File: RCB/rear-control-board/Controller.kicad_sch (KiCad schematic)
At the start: 23 parts, among them J6 Conn_01x05, U1 STM32F413CGUx, U2 LD1117S33TR_SOT223, U4 MCP2551-I-SN, Y1 CSTNE8M00

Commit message: willem review notes
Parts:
- added R?: 0, symbol Device:R
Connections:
- net +3V3: no longer U4.3 (VDD)
- net GND: now also R?.1; no longer U1.44 (BOOT0)
- new net: R?.2, U1.44 (BOOT0)
- new net +5V: U4.3 (VDD)
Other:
- note added: "Change these, the voltage divider stuff will be on the fault latcher sheet"
- note added: "add NC pins"
- note added: "add tsv to every signal pin including CAN -> use NUP2105LT1G or similar alternate The transceiver may have this built in, so double check"
- note added: "change to tx and rx and don't do differential pair"
- note added: "check pins for 5v tolerance actually, just do a different transceiver"
- note added: "check pull down value with ntc"
- note added: "choose a different tranceiver - one that has a vio pin that can set voltage - 3v tranceiver - level shifter - open drain on stm32 and pull up to 5v Look at MAX33054EASA+T"
- note added: "double check datasheet probably don't need this"
- note added: "header: FTSH-105-01-F-DV-K"
- note added: "seprate out ground and make it look pretty"
- note added: "vdd is 5v"
- note added: "why is is bold??"
- moved on the sheet: R4, R7

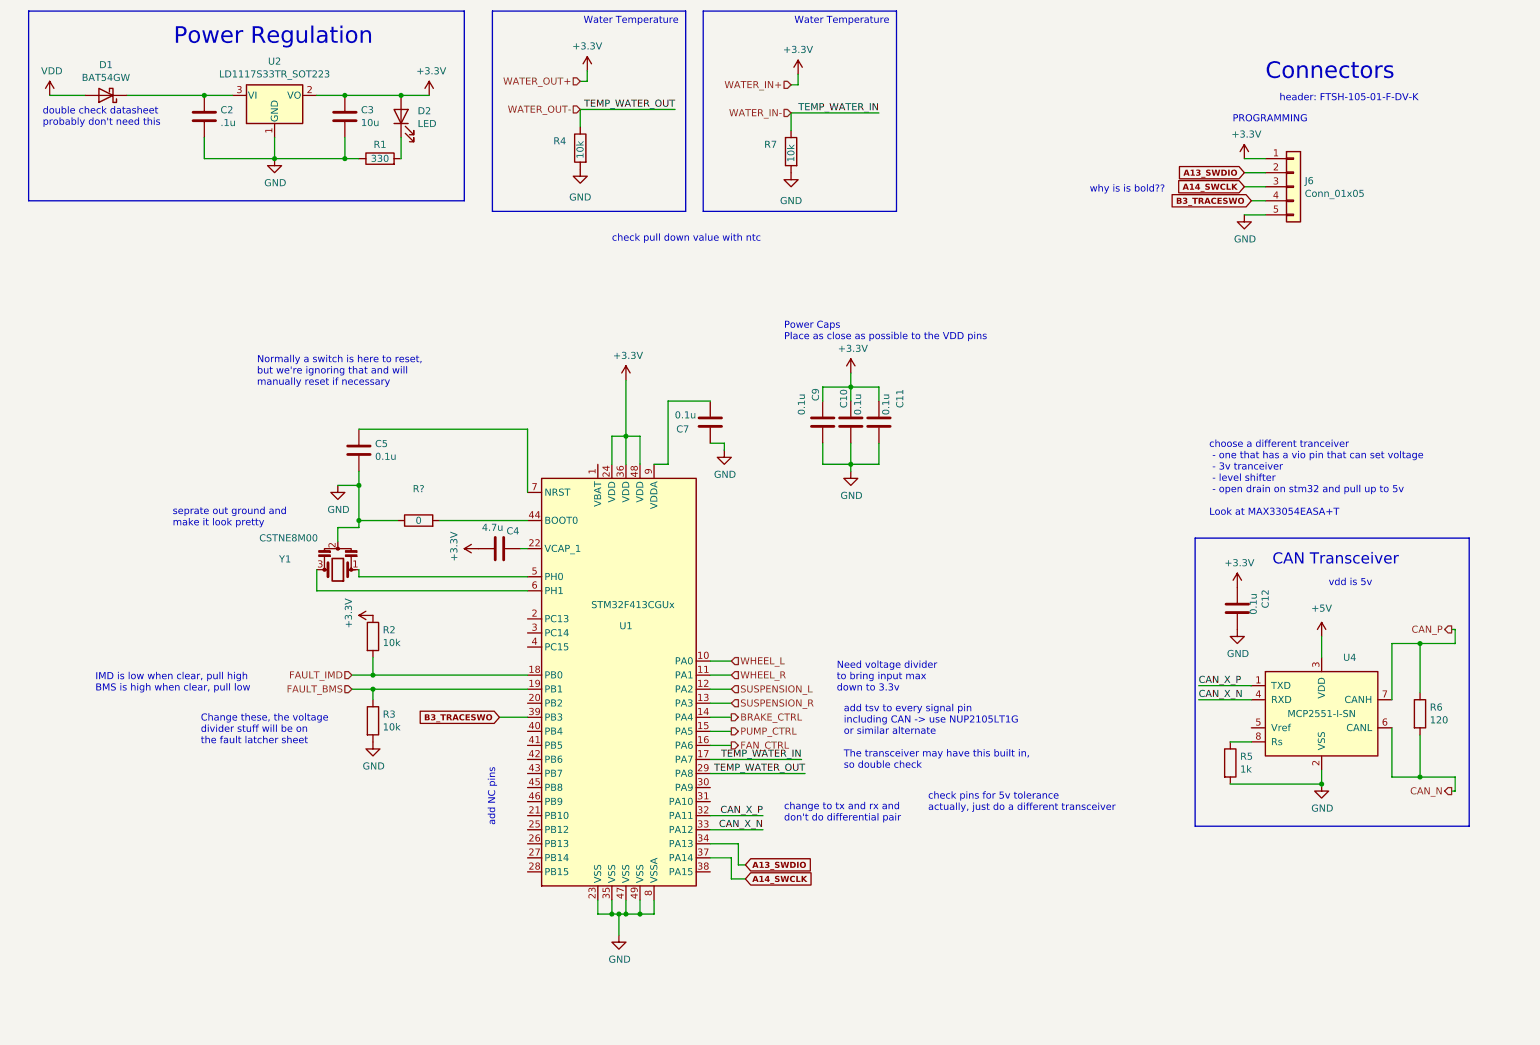
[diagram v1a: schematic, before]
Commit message: updating schem with design notes (major changes)
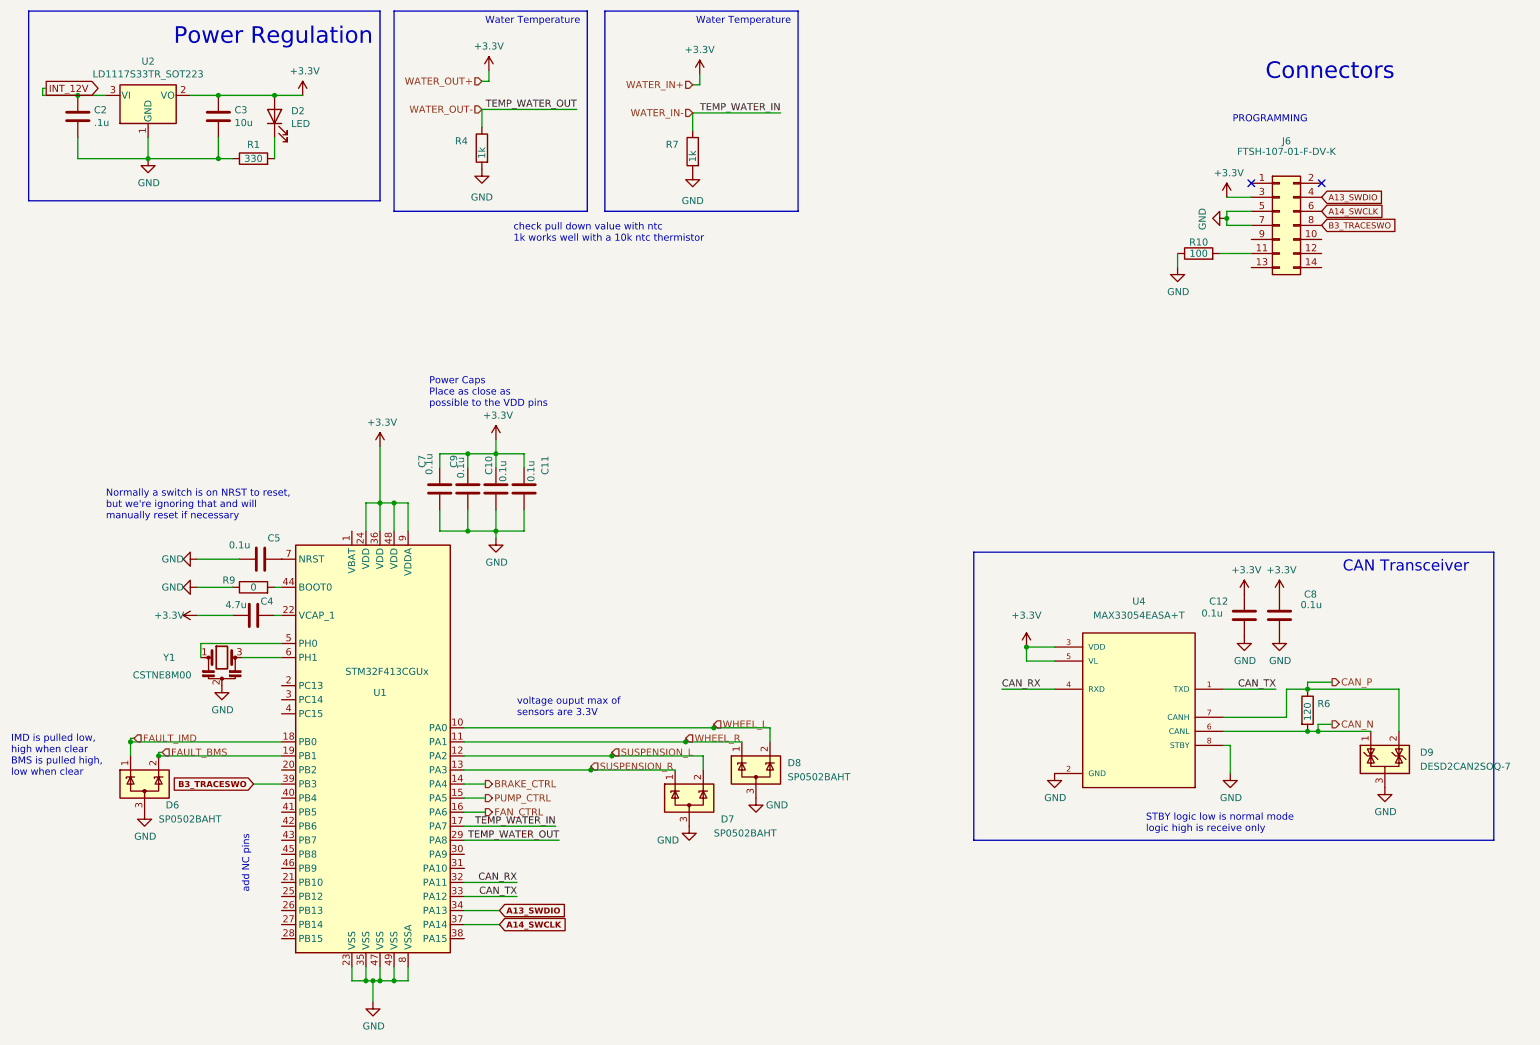
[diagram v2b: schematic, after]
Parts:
- removed D1: BAT54GW, Diode_SMD:D_SMB, symbol Device:D_Schottky
- removed J6: Conn_01x05, Connector_JST:JST_XH_B5B-XH-A_1x05_P2.50mm_Vertical, symbol Connector_Generic:Conn_01x05
- removed R2, R3: 10k, Resistor_SMD:R_0603_1608Metric_Pad0.98x0.95mm_HandSolder, symbol Device:R
- removed R5: 1k, Resistor_SMD:R_0603_1608Metric_Pad0.98x0.95mm_HandSolder, symbol Device:R
- removed U4: MCP2551-I-SN, Package_SO:SOIC-8_3.9x4.9mm_P1.27mm, symbol Interface_CAN_LIN:MCP2551-I-SN
- added C8: 0.1u, Capacitor_SMD:C_0603_1608Metric_Pad1.08x0.95mm_HandSolder, symbol Device:C
- added D6, D7, D8: SP0502BAHT, Package_TO_SOT_SMD:SOT-23, symbol Power_Protection:SP0502BAHT
- added D9: DESD2CAN2SOQ-7, Package_TO_SOT_SMD:SOT-23, symbol Power_Protection:NUP2105L
- added J6: FTSH-107-01-F-DV-K, Connector_PinHeader_1.27mm:PinHeader_2x07_P1.27mm_Vertical_SMD, symbol Connector_Generic:Conn_02x07_Odd_Even
- added R10: 100, Resistor_SMD:R_0603_1608Metric_Pad0.98x0.95mm_HandSolder, symbol Device:R
- added U4: MAX33054EASA+T, AERO_Footprints:SOIC127P600X175-8N, symbol AERO_Symbols:MAX33054EASA+T
- R4, R7: value 10k -> 1k
- R9: renamed from R?; footprint (none) -> Resistor_SMD:R_0603_1608Metric_Pad0.98x0.95mm_HandSolder
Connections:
- net +3V3: now also C7.1, U1.9 (VDDA), C8.1, J6.3 (Pin_3), U4.3 (VDD), U4.5 (VL)
- net A13_SWDIO: now also J6.4 (Pin_4)
- net A14_SWCLK: now also J6.6 (Pin_6)
- net B3_TRACESWO: now also J6.8 (Pin_8)
- net CAN_N: now also D9.1 (K), U4.6 (CANL)
- net CAN_P: now also D9.2 (K), U4.7 (CANH)
- net FAULT_BMS: now also D6.2 (K)
- net FAULT_IMD: now also D6.1 (K)
- net GND: now also C7.2, C8.2, D6.3 (A), D7.3 (A), D8.3 (A), D9.3 (A), J6.5 (Pin_5), J6.7 (Pin_7), R10.1, U4.2 (GND), U4.8 (STBY); no longer C7.1
- net SUSPENSION_L: now also D7.2 (K)
- net SUSPENSION_R: now also D7.1 (K)
- net WHEEL_L: now also D8.2 (K)
- net WHEEL_R: now also D8.1 (K)
- net INT_12V: now reaches C2.1, U2.3 (VI)
- net CAN_X_N renamed CAN_TX
- net CAN_TX: now also U4.1 (TXD)
- net CAN_X_P renamed CAN_RX
- net CAN_RX: now also U4.4 (RXD)
- new net: J6.11 (Pin_11), R10.2
- no-connect marks 0 -> 2
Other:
- note added: "IMD is pulled low, high when clear BMS is pulled high, low when clear"
- note added: "Normally a switch is on NRST to reset, but we're ignoring that and will manually reset if necessary"
- note added: "STBY logic low is normal mode logic high is receive only"
- note added: "check pull down value with ntc 1k works well with a 10k ntc thermistor"
- note added: "voltage ouput max of sensors are 3.3V"
- note removed: "Change these, the voltage divider stuff will be on the fault latcher sheet"
- note removed: "IMD is low when clear, pull high BMS is high when clear, pull low"
- note removed: "Need voltage divider to bring input max down to 3.3v"
- note removed: "Normally a switch is here to reset, but we're ignoring that and will manually reset if necessary"
- note removed: "add tsv to every signal pin including CAN -> use NUP2105LT1G or similar alternate The transceiver may have this built in, so double check"
- note removed: "change to tx and rx and don't do differential pair"
- note removed: "check pins for 5v tolerance actually, just do a different transceiver"
- note removed: "check pull down value with ntc"
- note removed: "choose a different tranceiver - one that has a vio pin that can set voltage - 3v tranceiver - level shifter - open drain on stm32 and pull up to 5v Look at MAX33054EASA+T"
- note removed: "double check datasheet probably don't need this"
- note removed: "header: FTSH-105-01-F-DV-K"
- note removed: "seprate out ground and make it look pretty"
- note removed: "vdd is 5v"
- note removed: "why is is bold??"
- moved on the sheet: C10, C11, C12, C2, C3, C4, C5, C9, D2, R1, R4, R6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

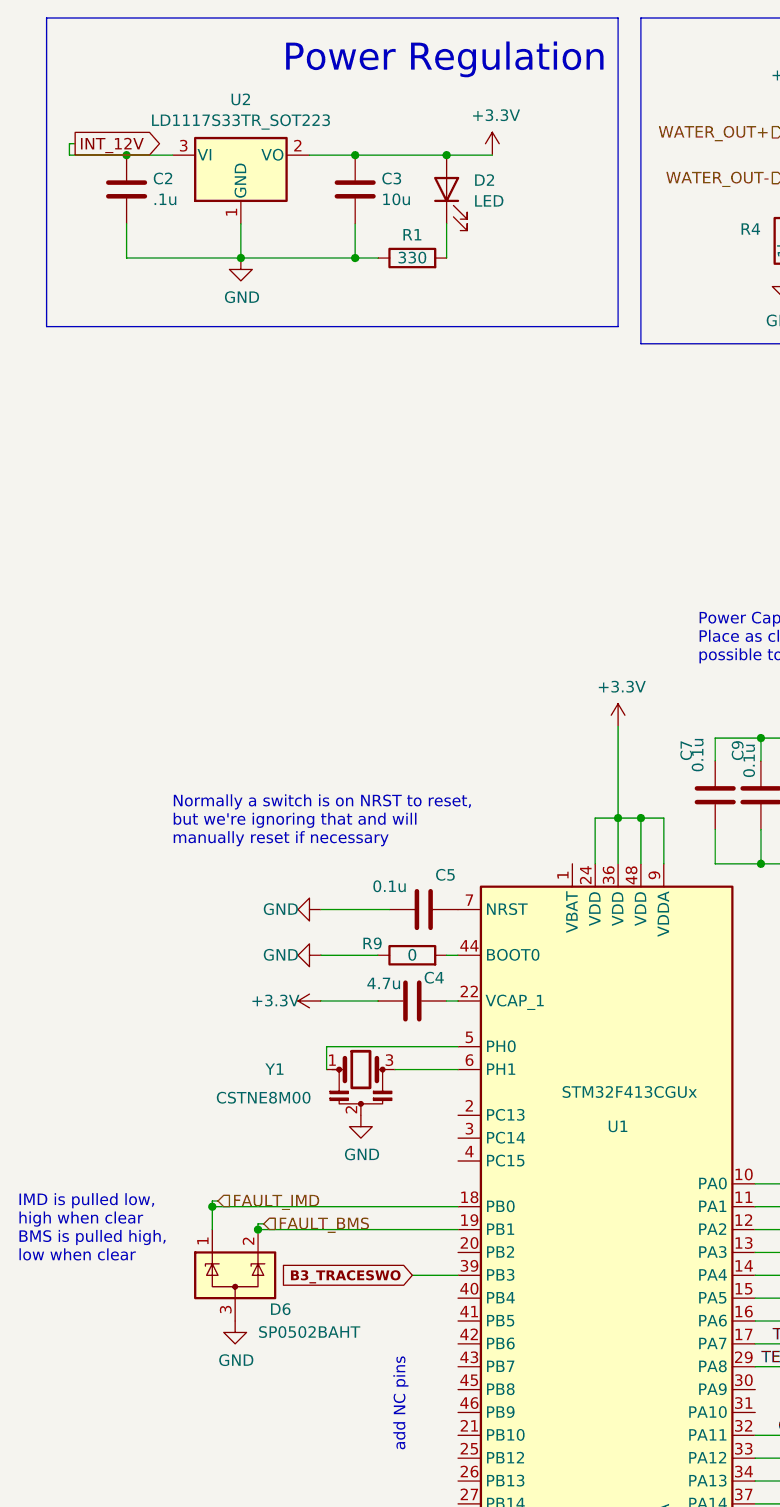
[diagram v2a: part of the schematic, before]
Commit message: minor layout changes based on schem updates
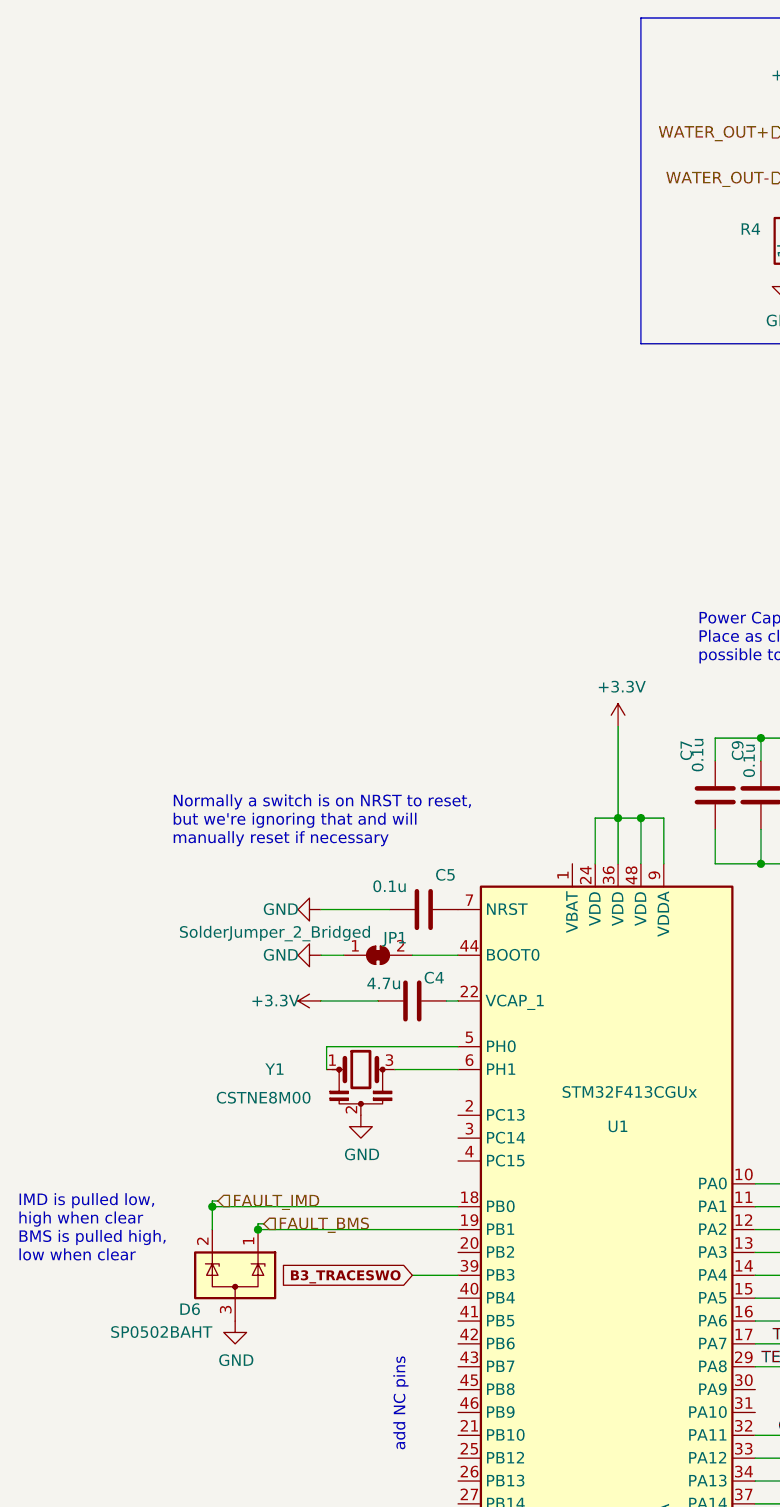
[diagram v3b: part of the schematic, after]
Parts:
- removed C2: .1u, Capacitor_SMD:C_0603_1608Metric_Pad1.08x0.95mm_HandSolder, symbol Device:C
- removed C3: 10u, Capacitor_SMD:C_0603_1608Metric_Pad1.08x0.95mm_HandSolder, symbol Device:C
- removed D2: LED, LED_SMD:LED_0603_1608Metric_Pad1.05x0.95mm_HandSolder, symbol Device:LED
- removed R1: 330, Resistor_SMD:R_0603_1608Metric_Pad0.98x0.95mm_HandSolder, symbol Device:R
- removed R9: 0, Resistor_SMD:R_0603_1608Metric_Pad0.98x0.95mm_HandSolder, symbol Device:R
- removed U2: LD1117S33TR_SOT223, Package_TO_SOT_SMD:SOT-223-3_TabPin2, symbol Regulator_Linear:LD1117S33TR_SOT223
- added JP1: SolderJumper_2_Bridged, Jumper:SolderJumper-2_P1.3mm_Bridged_Pad1.0x1.5mm, symbol Jumper:SolderJumper_2_Bridged
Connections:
- net FAULT_BMS: now also D6.1 (K); no longer D6.2 (K)
- net FAULT_IMD: now also D6.2 (K); no longer D6.1 (K)
- net GND: now also JP1.1 (A)
- net at U1.44 (BOOT0): now also JP1.2 (B)
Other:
- note removed: "Power Regulation"
